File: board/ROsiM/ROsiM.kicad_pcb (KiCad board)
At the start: 2 copper layers, 170.2 x 78.7 mm, 93 parts, among them J1 AVR-ISP-6, J2 RS232, J3 Power IN, J4 EXT_ADDR, J5 EXT_D, J6 External ~RESET, J7 External RESET, Q1 2N3904, Q2 2N3906, SW1 SW_Push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

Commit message: Updating for 1.2 PCB
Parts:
- added U21: 74HC04, Package_DIP:DIP-14_W7.62mm, F.Cu at (125.7, 85.1)
- moved C22 111.6 mm to (134.6, 81.3)
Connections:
- R24 pad 1: /MCU_RESET -> /ERST
- R30 pad 1: /MCU_RESET -> /~ERST
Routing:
- net /ERST: track 0.00 -> 97.6 mm, vias 0 -> 1
- net /~ERST: track 0.00 -> 81.1 mm, vias 0 -> 3
- net /~EXT_EN: track 210.7 -> 281.9 mm
- net /PISO_SER: track 83.4 -> 120.4 mm, vias 3 -> 2
- net /MCU_RESET: track 16.2 -> 52.3 mm, vias 0 -> 2
- net GND: track 880.9 -> 915.1 mm, vias 0 -> 1
- net /~SRAM_CE_MCU: track 142.9 -> 170.3 mm, vias 2 -> 4
- net /TTL-RX: track 36.3 -> 45.3 mm
- net /~SRAM_WE: track 109.1 -> 116.7 mm, vias 1 -> 2
- net /SRAM_A5: track 207.3 -> 214.4 mm
- net VCC: track 737.0 -> 730.3 mm
- net /SRAM_A16: track 153.8 -> 158.5 mm, vias 3 -> 4
- net /~PISO_CLR: track 79.9 -> 84.0 mm
- net /SRAM_A17: track 160.2 -> 164.0 mm, vias 2 -> 4
- net /SRAM_A8: track 156.5 -> 159.8 mm
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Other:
- board text added: "rev. 1.2"
- board text removed: "rev. 1.1"

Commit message: Begin designing rev 1.3
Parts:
- removed C4, C5, C6, C7: 1.0uF, Capacitor_THT:CP_Radial_D5.0mm_P2.50mm
- removed J3: Power IN, Connector_BarrelJack:BarrelJack_Horizontal
- removed SW2: Power, EproSim:Slide_Switch
- removed U7: L7805, Package_TO_SOT_THT:TO-220-3_Horizontal_TabDown
- added D4: RX, LED_THT:LED_D2.0mm_W4.8mm_H2.5mm_FlatTop, F.Cu at (127.0, 61.0)
- added F1: 500mA, Fuse:Fuse_1206_3216Metric, F.Cu at (96.5, 66.0)
- added JP1: VCCIO sel, Jumper:SolderJumper-2_P1.3mm_Open_RoundedPad1.0x1.5mm, F.Cu at (118.1, 76.2)
- added R31: 470, Resistor_THT:R_Axial_DIN0204_L3.6mm_D1.6mm_P7.62mm_Horizontal, F.Cu at (130.8, 58.4)
- added R32: 470, Resistor_THT:R_Axial_DIN0204_L3.6mm_D1.6mm_P7.62mm_Horizontal, F.Cu at (130.8, 61.0)
- C15: value 0.22uF -> 10uF
- D3: value 1N4001 -> TX; footprint Diode_THT:D_DO-41_SOD81_P10.16mm_Horizontal -> LED_THT:LED_D2.0mm_W4.8mm_H2.5mm_FlatTop
- J2: value RS232 -> USB_B; footprint Connector_Dsub:DSUB-9_Female_Horizontal_P2.77x2.84mm_EdgePinOffset4.94mm_Housed_MountingHolesOffset7.48mm -> Connector_USB:USB_B_Lumberg_2411_02_Horizontal
- R17: value 1.2K -> 1K
- U6: value MAX232 -> FT232RL; footprint Package_DIP:DIP-16_W7.62mm -> Package_SO:SSOP-28_5.3x10.2mm_P0.65mm
- moved C15 66.5 mm to (101.6, 73.7)
- moved D3 61.1 mm to (123.2, 61.0), turned to 90 degrees
- moved C14 46.6 mm to (118.1, 68.6), turned to 270 degrees
- moved D2 31.9 mm to (143.5, 61.0), turned to 90 degrees
- moved R17 25.7 mm to (147.3, 58.4)
- moved C10 10.9 mm to (109.2, 80.0)
- moved C3 8.03 mm to (120.7, 68.6), turned to 270 degrees
- moved J2 5.24 mm to (109.2, 64.8), turned to 90 degrees
- moved U6 5.24 mm to (110.5, 72.4)
- moved C22 2.54 mm to (132.1, 81.3)
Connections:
- C14 pad 1: VCC -> GND
- C14 pad 2: GND -> +3V3
- C15 pad 1: /RECT_V12 -> GND
- C15 pad 2: GND -> VCC
- C3 pad 1: /~RESET -> GND
- C3 pad 2: Net-(C3-Pad2) -> VCC
- D2 pad 2: /RECT_V12 -> VCC
- D3 pad 1: /RECT_V12 -> Net-(D3-Pad1)
- D3 pad 2: /SW_12V -> Net-(D3-Pad2)
- J2 pad 1: (no net) -> Net-(F1-Pad2)
- J2 pad 2: /RS232-RX -> Net-(J2-Pad2)
- J2 pad 3: /RS232-TX -> Net-(J2-Pad3)
- J2 pad 4: /RS232-DTR -> GND
- U6 pad 1: Net-(C4-Pad1) -> /TTL-RX
- U6 pad 10: /TTL-TX -> (no net)
- U6 pad 11: GND -> (no net)
- U6 pad 12: Net-(C3-Pad2) -> (no net)
- U6 pad 13: /RS232-DTR -> (no net)
- U6 pad 15: GND -> Net-(J2-Pad3)
- U6 pad 16: VCC -> Net-(J2-Pad2)
- U6 pad 2: Net-(C6-Pad1) -> /~RESET
- U6 pad 3: Net-(C4-Pad2) -> (no net)
- U6 pad 5: Net-(C5-Pad2) -> /TTL-TX
- U6 pad 6: Net-(C7-Pad2) -> (no net)
- U6 pad 7: /RS232-RX -> GND
- U6 pad 8: /RS232-TX -> (no net)
- U6 pad 9: /TTL-RX -> (no net)
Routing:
- net GND: track 915.1 -> 1010.7 mm, vias 1 -> 2
- net /~EXT_EN: track 281.9 -> 227.4 mm, vias 1 -> 3
- net VCC: track 730.3 -> 774.8 mm, vias 3 -> 5
- net /SRAM_A5: track 214.4 -> 172.8 mm
- net /RECT_V12: track 35.0 -> 0.00 mm
- net Net-(D3-Pad1): track 0.00 -> 29.2 mm, vias 0 -> 1
- net Net-(D4-Pad1): track 0.00 -> 29.1 mm
- net /RS232-TX: track 24.8 -> 0.00 mm
- net /RS232-RX: track 17.2 -> 0.00 mm
- net +12V: track 16.5 -> 0.00 mm
- net /TTL-RX: track 45.3 -> 30.2 mm, vias 0 -> 1
- net Net-(C3-Pad2): track 13.9 -> 0.00 mm
- net /~RESET: track 54.4 -> 40.4 mm
- net Net-(F1-Pad2): track 0.00 -> 12.8 mm
- net Net-(C6-Pad1): track 12.0 -> 0.00 mm
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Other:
- board text added: "HI"
- board text added: "LO"
- board text added: "rev. 1.3"
- board text removed: "7-9V TIP positive"
- board text removed: "Power"
- board text removed: "Power Switch"
- board text removed: "rev. 1.2"

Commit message: Updated readme and 1.3 pcb
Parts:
- added C29: 100nF, Capacitor_THT:C_Disc_D3.4mm_W2.1mm_P2.50mm, F.Cu at (102.9, 77.5)
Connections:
- U6 pad 2: /~RESET -> Net-(C29-Pad1)
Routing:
- net /~RESET: track 40.4 -> 32.1 mm
- net Net-(C29-Pad1): track 0.00 -> 6.26 mm
- net /ERST: track 97.6 -> 99.9 mm
- net VCC: track 774.8 -> 776.6 mm

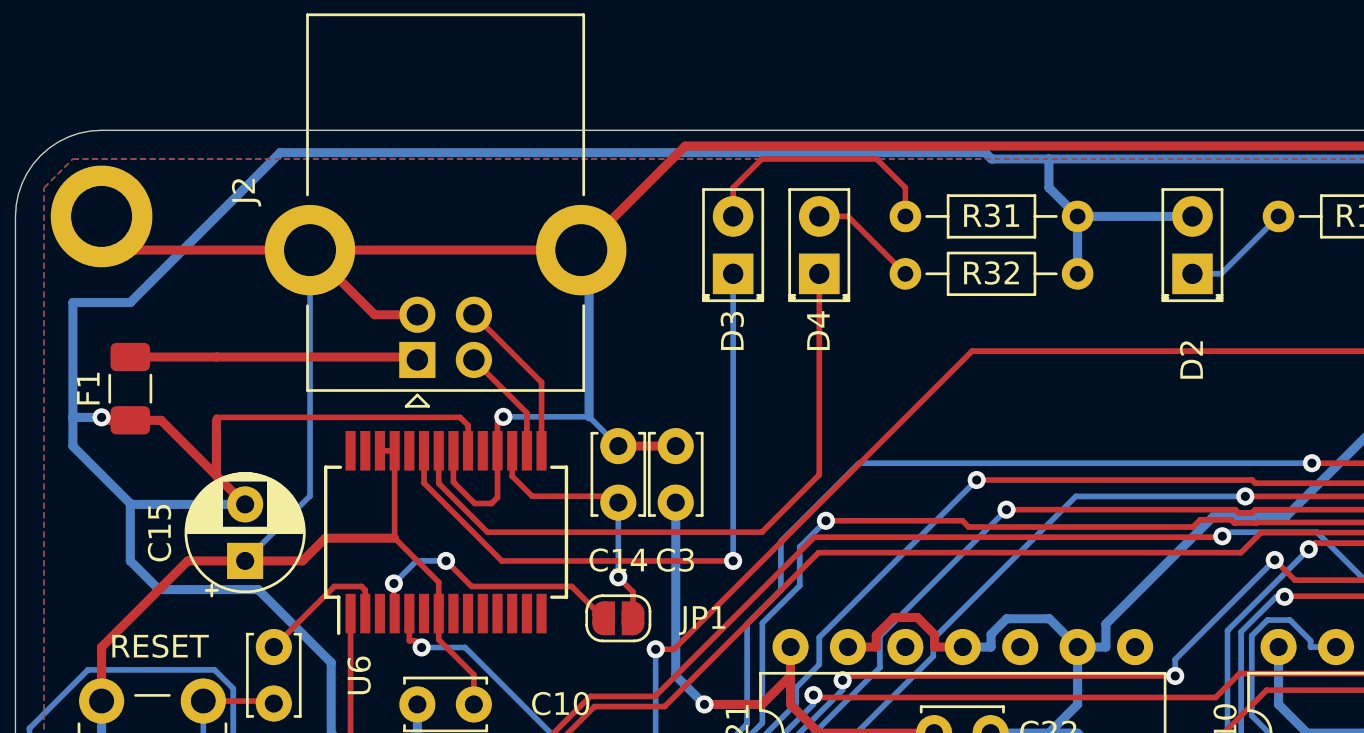
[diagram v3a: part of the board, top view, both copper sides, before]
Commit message: Whoops, a cap was inverted
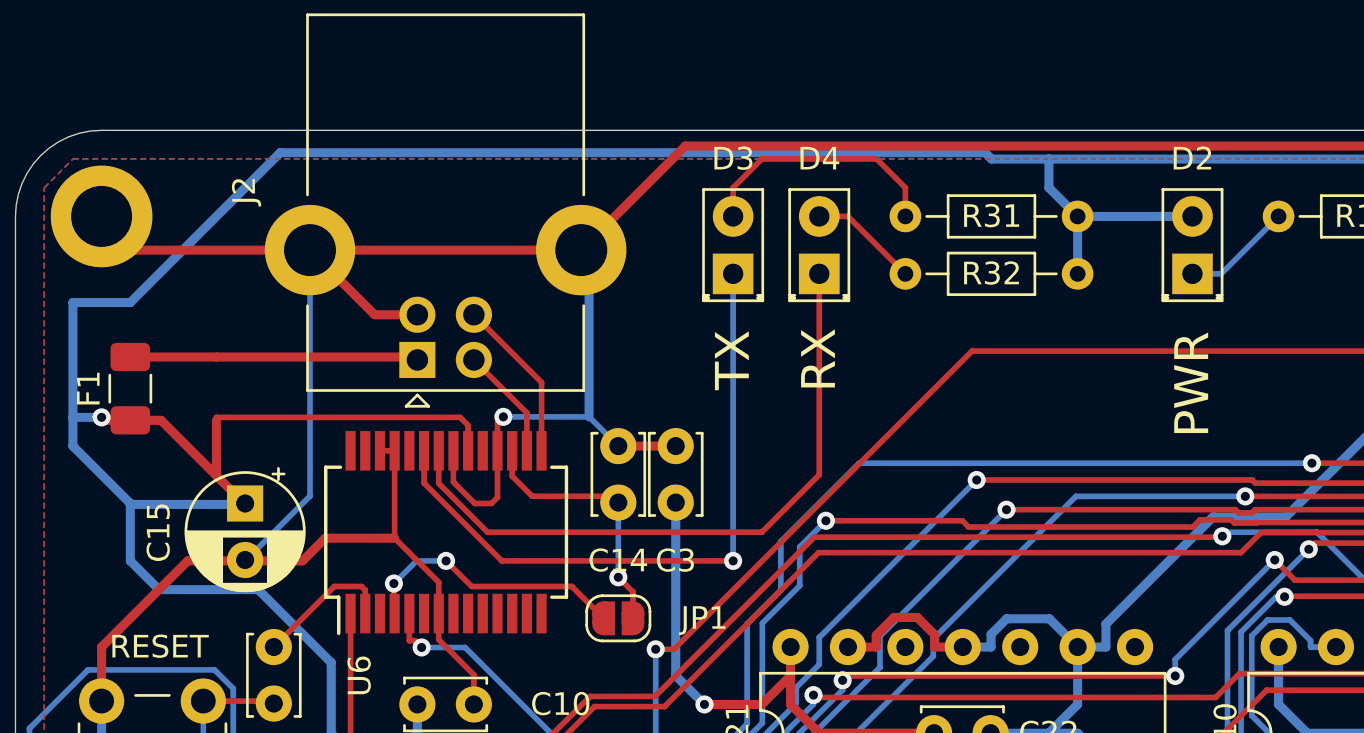
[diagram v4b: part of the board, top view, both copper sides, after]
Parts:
- moved C15 2.54 mm to (101.6, 71.1), turned to 270 degrees
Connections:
- C15 pad 1: GND -> VCC
- C15 pad 2: VCC -> GND
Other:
- board text added: "PWR"
- board text added: "RX"
- board text added: "TX"
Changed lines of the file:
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@@
   (general
     (thickness 1.6)
-    (drawings 64)
+    (drawings 67)
     (tracks 3432)
     (zones 0)
@@
   (layers
     (0 F.Cu signal)
-    (31 B.Cu signal)
+    (31 B.Cu signal hide)
     (32 B.Adhes user)
     (33 F.Adhes user)
@@
     (add_net "Net-(U11-Pad14)")
     (add_net "Net-(U11-Pad9)")
-    (add_net "Net-(U12-Pad3)")
-    (add_net "Net-(U12-Pad4)")
-    (add_net "Net-(U12-Pad5)")
-    (add_net "Net-(U12-Pad6)")
-    (add_net "Net-(U12-Pad7)")
-    (add_net "Net-(U12-Pad9)")
     (add_net "Net-(U15-Pad12)")
-    (add_net "Net-(U18-Pad3)")
-    (add_net "Net-(U18-Pad5)")
-    (add_net "Net-(U18-Pad7)")
     (add_net "Net-(U2-Pad9)")
-    (add_net "Net-(U21-Pad10)")
-    (add_net "Net-(U21-Pad12)")
-    (add_net "Net-(U21-Pad6)")
-    (add_net "Net-(U21-Pad8)")
     (add_net "Net-(U3-Pad9)")
-    (add_net "Net-(U6-Pad10)")
-    (add_net "Net-(U6-Pad11)")
-    (add_net "Net-(U6-Pad12)")
-    (add_net "Net-(U6-Pad13)")
-    (add_net "Net-(U6-Pad14)")
-    (add_net "Net-(U6-Pad19)")
-    (add_net "Net-(U6-Pad27)")
-    (add_net "Net-(U6-Pad28)")
-    (add_net "Net-(U6-Pad3)")
-    (add_net "Net-(U6-Pad6)")
-    (add_net "Net-(U6-Pad9)")
   )
   (net_class POWER ""
@@
     (descr "LED, Round, FlatTop,  Rectangular size 4.8x2.5mm^2 diameter 2.0mm, 2 pins, http://www.kingbright.com/attachments/file/psearch/000/00/00/L-13GD(Ver.11B).pdf")
     (tags "LED Round FlatTop  Rectangular size 4.8x2.5mm^2 diameter 2.0mm 2 pins")
-    (fp_text reference D4 (at -2.54 0 90) (layer F.SilkS)
+    (fp_text reference D4 (at 5.08 0) (layer F.SilkS)
       (effects (font (size 1 1) (thickness 0.15)))
     )
@@
     (descr "LED, Round, FlatTop,  Rectangular size 4.8x2.5mm^2 diameter 2.0mm, 2 pins, http://www.kingbright.com/attachments/file/psearch/000/00/00/L-13GD(Ver.11B).pdf")
     (tags "LED Round FlatTop  Rectangular size 4.8x2.5mm^2 diameter 2.0mm 2 pins")
-    (fp_text reference D3 (at -2.54 0 90) (layer F.SilkS)
+    (fp_text reference D3 (at 5.08 0) (layer F.SilkS)
       (effects (font (size 1 1) (thickness 0.15)))
     )
@@
     (descr "LED, Round, FlatTop,  Rectangular size 4.8x2.5mm^2 diameter 2.0mm, 2 pins, http://www.kingbright.com/attachments/file/psearch/000/00/00/L-13GD(Ver.11B).pdf")
     (tags "LED Round FlatTop  Rectangular size 4.8x2.5mm^2 diameter 2.0mm 2 pins")
-    (fp_text reference D2 (at -3.81 0 90) (layer F.SilkS)
+    (fp_text reference D2 (at 5.08 0) (layer F.SilkS)
       (effects (font (size 1 1) (thickness 0.15)))
     )
@@
   )
   (module Capacitor_THT:CP_Radial_D5.0mm_P2.50mm (layer F.Cu)
-    (at 101.6 73.66 90)
+    (at 101.6 71.12 270)
     (descr "CP, Radial series, Radial, pin pitch=2.50mm, , diameter=5mm, Electrolytic Capacitor")
     (tags "CP Radial series Radial pin pitch 2.50mm  diameter 5mm Electrolytic Capacitor")
-    (fp_text reference C15 (at 1.25 -3.75 90) (layer F.SilkS)
+    (fp_text reference C15 (at 1.27 3.81 90) (layer F.SilkS)
       (effects (font (size 1 1) (thickness 0.15)))
     )
@@
       (effects (font (size 1 1) (thickness 0.15)))
     )
-    (pad 2 thru_hole circle (at 2.5 0 90) (size 1.6 1.6) (drill 0.8) (layers *.Cu *.Mask)
-      (net 5 VCC))
-    (pad 1 thru_hole rect (at 0 0 90) (size 1.6 1.6) (drill 0.8) (layers *.Cu *.Mask)
+    (pad 2 thru_hole circle (at 2.5 0 270) (size 1.6 1.6) (drill 0.8) (layers *.Cu *.Mask)
       (net 2 GND))
+    (pad 1 thru_hole rect (at 0 0 270) (size 1.6 1.6) (drill 0.8) (layers *.Cu *.Mask)
+      (net 5 VCC))
     (model ${KISYS3DMOD}/Capacitor_THT.3dshapes/CP_Radial_D5.0mm_P2.50mm.wrl
       (at (xyz 0 0 0))
@@
     )
   )
+  (gr_text PWR (at 143.51 63.5 90) (layer F.SilkS)
+    (effects (font (size 1.5 1.5) (thickness 0.3)) (justify right))
+  )
+  (gr_text RX (at 127 64.77 90) (layer F.SilkS)
+    (effects (font (size 1.5 1.5) (thickness 0.3)))
+  )
+  (gr_text TX (at 123.19 64.77 90) (layer F.SilkS)
+    (effects (font (size 1.5 1.5) (thickness 0.3)))
+  )
   (gr_text HI (at 199.39 69.85) (layer F.SilkS)

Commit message: Update ROsiM design
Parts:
- removed JP1: VCCIO sel, Jumper:SolderJumper-2_P1.3mm_Open_RoundedPad1.0x1.5mm
- U1: value ATmega8A-PU -> ATmega328P
- Y1: value 8Mhz -> 20Mhz
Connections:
- U6 pad 4: Net-(JP1-Pad1) -> VCC
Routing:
- net Net-(JP1-Pad1): track 12.1 -> 0.00 mm, vias 2 -> 0
- net +3V3: track 11.7 -> 6.30 mm, vias 1 -> 0
- net VCC: track 776.6 -> 781.3 mm
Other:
- board text added: "rev. 1.4"
- board text removed: "rev. 1.3"
